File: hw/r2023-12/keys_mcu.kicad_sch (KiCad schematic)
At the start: 29 parts, among them J3 Conn_01x26_Socket, J5 Conn_ARM_JTAG_SWD_10, J6 Conn_01x06_Socket, SW1 PWR, SW2 MUTE, SW2 Volume, SW3 PREV, SW4 PLAY_PAUSE, SW5 NEXT, U2 STM32G431CBUx

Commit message: r2023-12: add row/column notes
We got valuable notes from: https://github.com/qmk/qmk_firmware/blob/master/keyboards/handwired/daskeyboard/daskeyboard4/info.json

We don't have a fully working keyboard yet, but it's nearly there.
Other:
- note added: "NC!"
- note added: "row"
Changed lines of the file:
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@@
     (stroke (width 0) (type default))
+  )
+  (text "NC!" (at 50.8 147.32 0)
+    (effects (font (size 1.27 1.27)) (justify left bottom))
   )
   (text "Must be _low_ to boot normally. high for DFU\nand we don't want to interfere with canfd?\n=> If it interferes with CAN, we remove it,\nand use option bits to override boot0"
@@
     (effects (font (size 1.27 1.27)) (justify left bottom))
   )
+  (text "row" (at 50.8 104.14 0)
+    (effects (font (size 2 2)) (justify left bottom))
+  )
   (text "Power budget:\nLEDS 3x5mA => 15mA max\nMCU:\n * core: 44mA  @ 170MHZ full steam\n * all peripherals 250uA/Mhz @ 170MHZ => 43mA\n=> 100mA => 200mA is _plenty_ here....\nMCU allows 20mA / pin, max, theoretical, 100mA max.\nSo we're fine with 5mA leds, no matter how we slice/dice.\nMatrices use.... less?"
     (at -63.5 40.64 0)
     (effects (font (size 1.27 1.27)) (justify left bottom))
+  )
+  (text "row" (at 50.8 99.06 0)
+    (effects (font (size 2 2)) (justify left bottom))
   )
   (text "TODO: RC debounce?\nyolo?" (at 251.46 154.94 0)
@@
     (effects (font (size 1.27 1.27)) (justify left bottom))
   )
+  (text "row" (at 50.8 88.9 0)
+    (effects (font (size 2 2)) (justify left bottom))
+  )
+  (text "row" (at 50.8 144.78 0)
+    (effects (font (size 2 2)) (justify left bottom))
+  )
+  (text "row" (at 50.8 91.44 0)
+    (effects (font (size 2 2)) (justify left bottom))
+  )
   (text "Will probably want to experiment with\nviewing angle, max brightness, current.\nPins can be PWMd if need be...\n(At present, all pins except PF1 have timer alt functions)"
     (at 180.34 160.02 0)
     (effects (font (size 1.27 1.27)) (justify left bottom))
+  )
+  (text "row" (at 50.8 127 0)
+    (effects (font (size 2 2)) (justify left bottom))
   )
   (text "DS says 3x100nF + 1x4.7  just for vdd\nPLUS 1uF+100nF for vRef, plus 1uF+100nF for vdda.\n\nApp note says _mandatory_ is 1x100nF plus 1x4.7uF + 3x1uF!\n  (1x1uF on vef, 1 on vdda, and ..?\n  (ref diagram _doesn't_ do that)\n\nI think 3x100nF, plus 2x1uf is... plenty....\n1uF near vdda and vref?"
@@
     (effects (font (size 1.27 1.27)) (justify left bottom))
   )
+  (text "row" (at 50.8 139.7 0)
+    (effects (font (size 2 2)) (justify left bottom))
+  )
   (text "TIM2 channels 1/2, just in case\n" (at 170.18 60.96 0)
     (effects (font (size 1.27 1.27)) (justify left bottom))
   )
+  (text "row" (at 50.8 142.24 0)
+    (effects (font (size 2 2)) (justify left bottom))
+  )
   (text "Onboard pulldowns\nActive high" (at 248.92 88.9 0)

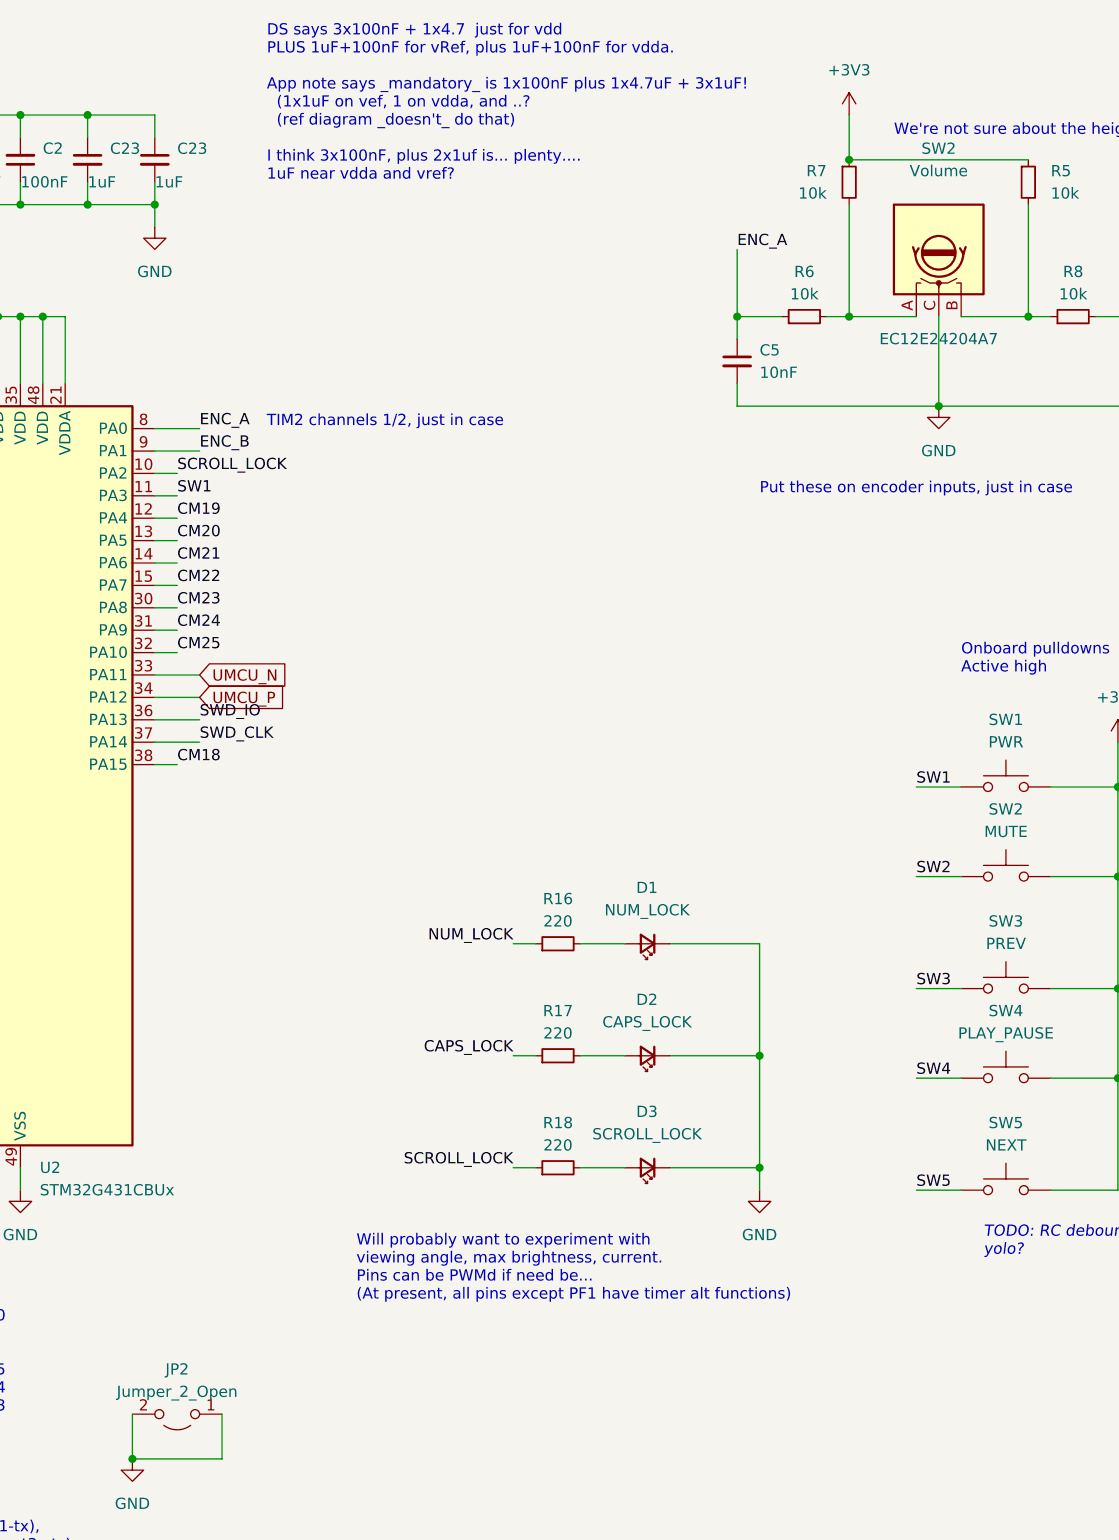
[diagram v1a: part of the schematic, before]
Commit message: r2023_12: add firmware notes and comments on matrix decode
No intentional changes, just text added while working out the firmware.
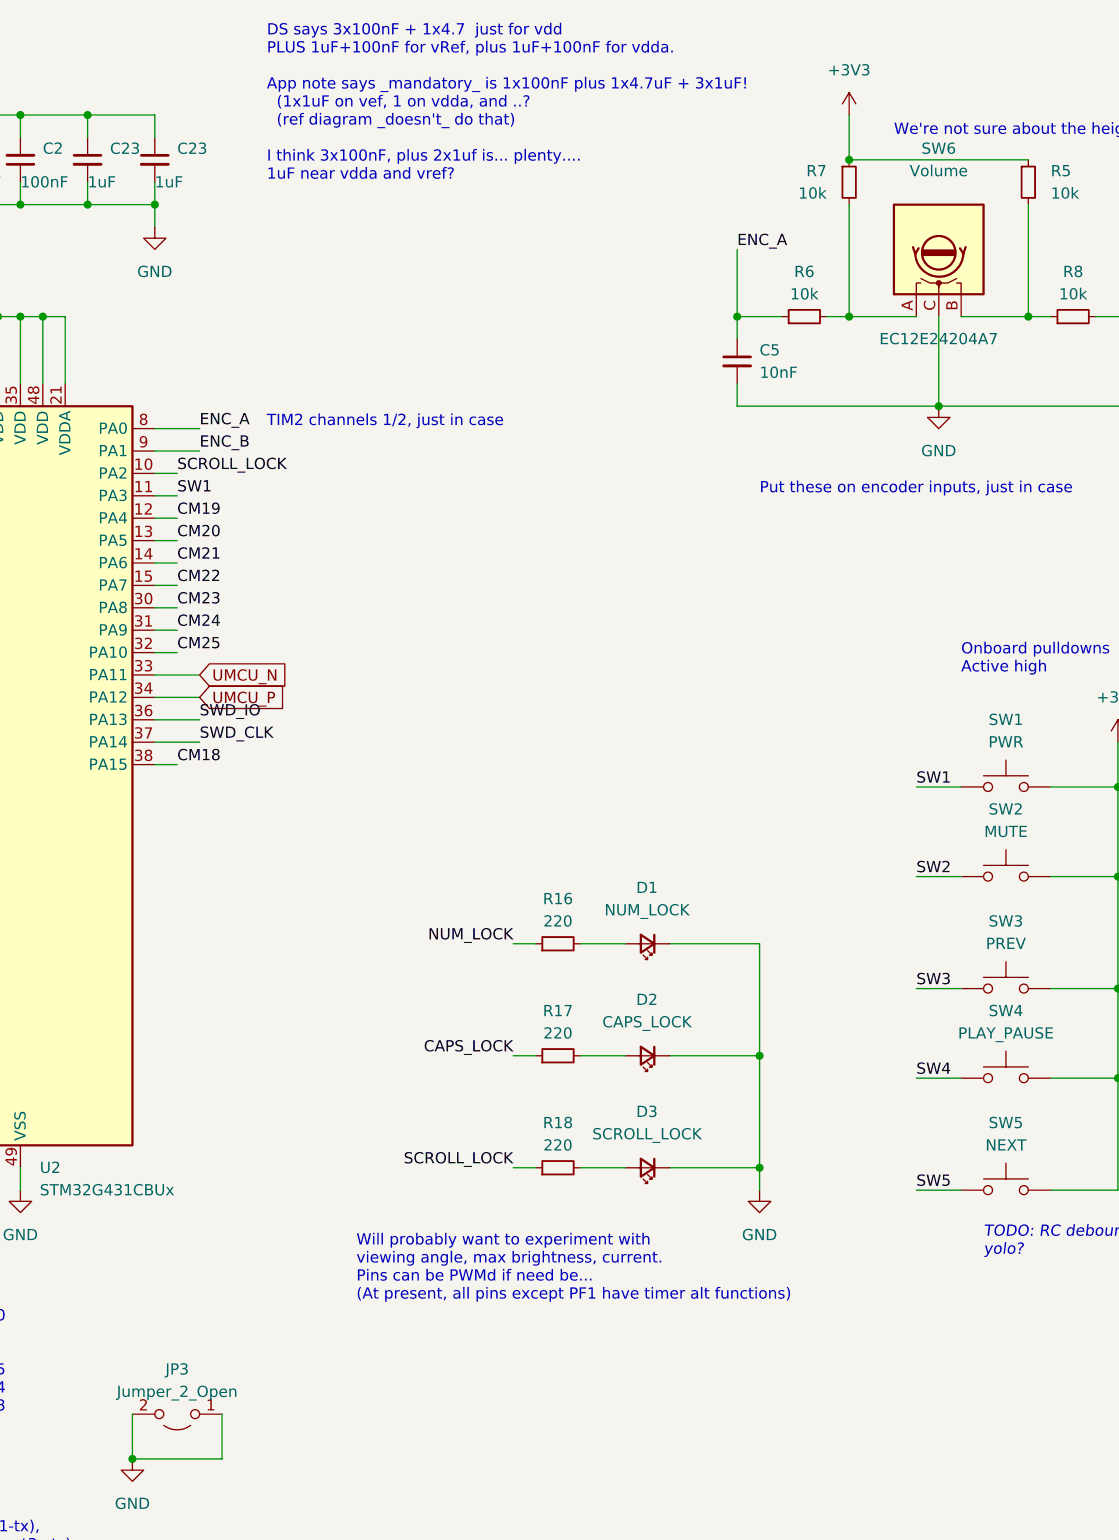
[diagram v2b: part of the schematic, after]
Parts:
- renumbered JP2 to JP3, SW2 to SW6
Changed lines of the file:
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@@
       )
       (project "das-kb4-bara2"
-        (path "/d0e4eaec-96cb-4a0e-a384-5b3e3f5f8d5d/f457a5c4-270e-459d-a4f0-150cf90e3909"
-          (reference "C1") (unit 1)
-        )
         (path "/d0e4eaec-96cb-4a0e-a384-5b3e3f5f8d5d/7c81bc9d-f306-4c7f-90ce-10f7b22818e4"
           (reference "C7") (unit 1)
@@
       )
       (project "das-kb4-bara2"
-        (path "/d0e4eaec-96cb-4a0e-a384-5b3e3f5f8d5d/f457a5c4-270e-459d-a4f0-150cf90e3909"
-          (reference "C1") (unit 1)
-        )
         (path "/d0e4eaec-96cb-4a0e-a384-5b3e3f5f8d5d/7c81bc9d-f306-4c7f-90ce-10f7b22818e4"
           (reference "C4") (unit 1)
@@
       )
       (project "das-kb4-bara2"
-        (path "/d0e4eaec-96cb-4a0e-a384-5b3e3f5f8d5d/f457a5c4-270e-459d-a4f0-150cf90e3909"
-          (reference "C10") (unit 1)
-        )
-        (path "/d0e4eaec-96cb-4a0e-a384-5b3e3f5f8d5d"
-          (reference "C13") (unit 1)
-        )
         (path "/d0e4eaec-96cb-4a0e-a384-5b3e3f5f8d5d/7c81bc9d-f306-4c7f-90ce-10f7b22818e4"
           (reference "C12") (unit 1)
@@
       )
       (project "das-kb4-bara2"
-        (path "/d0e4eaec-96cb-4a0e-a384-5b3e3f5f8d5d/f457a5c4-270e-459d-a4f0-150cf90e3909"
-          (reference "C1") (unit 1)
-        )
         (path "/d0e4eaec-96cb-4a0e-a384-5b3e3f5f8d5d/7c81bc9d-f306-4c7f-90ce-10f7b22818e4"
           (reference "C2") (unit 1)
@@
     (instances
       (project "das-kb4-bara2"
-        (path "/d0e4eaec-96cb-4a0e-a384-5b3e3f5f8d5d"
-          (reference "D3") (unit 1)
-        )
         (path "/d0e4eaec-96cb-4a0e-a384-5b3e3f5f8d5d/7c81bc9d-f306-4c7f-90ce-10f7b22818e4"
           (reference "D3") (unit 1)
@@
     (instances
       (project "das-kb4-bara2"
-        (path "/d0e4eaec-96cb-4a0e-a384-5b3e3f5f8d5d"
-          (reference "D1") (unit 1)
-        )
         (path "/d0e4eaec-96cb-4a0e-a384-5b3e3f5f8d5d/7c81bc9d-f306-4c7f-90ce-10f7b22818e4"
           (reference "D1") (unit 1)
@@
   (symbol (lib_id "Jumper:Jumper_2_Open") (at 160.02 172.72 180) (unit 1)
     (in_bom yes) (on_board yes) (dnp no) (fields_autoplaced)
-    (property "Reference" "JP2" (at 160.02 167.64 0)
+    (property "Reference" "JP3" (at 160.02 167.64 0)
       (effects (font (size 1.27 1.27)))
     )
@@
     (instances
       (project "das-kb4-bara2"
-        (path "/d0e4eaec-96cb-4a0e-a384-5b3e3f5f8d5d/a2d5569b-3e38-48fc-9c53-ff19306ffa54"
-          (reference "JP2") (unit 1)
-        )
         (path "/d0e4eaec-96cb-4a0e-a384-5b3e3f5f8d5d/7c81bc9d-f306-4c7f-90ce-10f7b22818e4"
           (reference "JP3") (unit 1)
@@
     (instances
       (project "das-kb4-bara2"
-        (path "/d0e4eaec-96cb-4a0e-a384-5b3e3f5f8d5d"
+        (path "/d0e4eaec-96cb-4a0e-a384-5b3e3f5f8d5d/7c81bc9d-f306-4c7f-90ce-10f7b22818e4"
           (reference "U2") (unit 1)
         )
-        (path "/d0e4eaec-96cb-4a0e-a384-5b3e3f5f8d5d/7c81bc9d-f306-4c7f-90ce-10f7b22818e4"
-          (reference "U2") (unit 1)
-        )
       )
     )
@@
     (instances
       (project "das-kb4-bara2"
-        (path "/d0e4eaec-96cb-4a0e-a384-5b3e3f5f8d5d"
-          (reference "D2") (unit 1)
-        )
         (path "/d0e4eaec-96cb-4a0e-a384-5b3e3f5f8d5d/7c81bc9d-f306-4c7f-90ce-10f7b22818e4"
           (reference "D2") (unit 1)
@@
       )
       (project "das-kb4-bara2"
-        (path "/d0e4eaec-96cb-4a0e-a384-5b3e3f5f8d5d/f457a5c4-270e-459d-a4f0-150cf90e3909"
-          (reference "C10") (unit 1)
-        )
-        (path "/d0e4eaec-96cb-4a0e-a384-5b3e3f5f8d5d"
-          (reference "C13") (unit 1)
-        )
         (path "/d0e4eaec-96cb-4a0e-a384-5b3e3f5f8d5d/7c81bc9d-f306-4c7f-90ce-10f7b22818e4"
           (reference "C8") (unit 1)
@@
   (symbol (lib_id "Device:RotaryEncoder") (at 246.38 40.64 90) (unit 1)
     (in_bom yes) (on_board yes) (dnp no)
-    (property "Reference" "SW2" (at 246.38 29.21 90)
+    (property "Reference" "SW6" (at 246.38 29.21 90)
       (effects (font (size 1.27 1.27)))
     )
@@
     (instances
       (project "das-kb4-bara2"
-        (path "/d0e4eaec-96cb-4a0e-a384-5b3e3f5f8d5d/f457a5c4-270e-459d-a4f0-150cf90e3909"
-          (reference "SW2") (unit 1)
-        )
         (path "/d0e4eaec-96cb-4a0e-a384-5b3e3f5f8d5d/7c81bc9d-f306-4c7f-90ce-10f7b22818e4"
           (reference "SW6") (unit 1)
